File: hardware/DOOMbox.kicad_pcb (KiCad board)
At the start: 4 copper layers, 129 parts, among them J1 DE15_Socket_HighDensity, J2 AudioJack3, SW1 SW_SPST, SW2 SW_Push, U1 RPi Pico 2, U3 AP7381-50SA-7, U4 LM324N, U5 CD4010BE

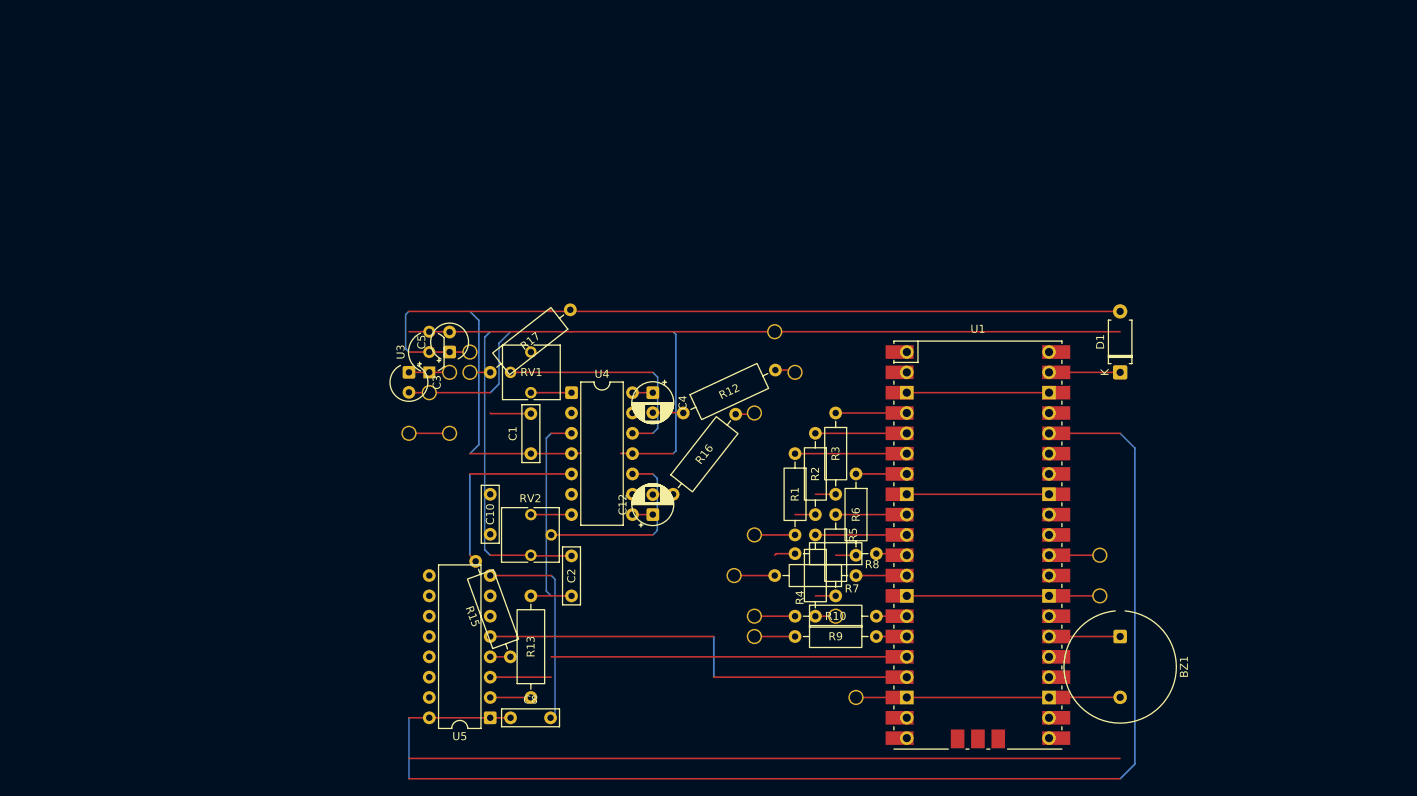
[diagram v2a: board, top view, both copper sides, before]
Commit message: Rework stripboard design (+ edit sb symbols)
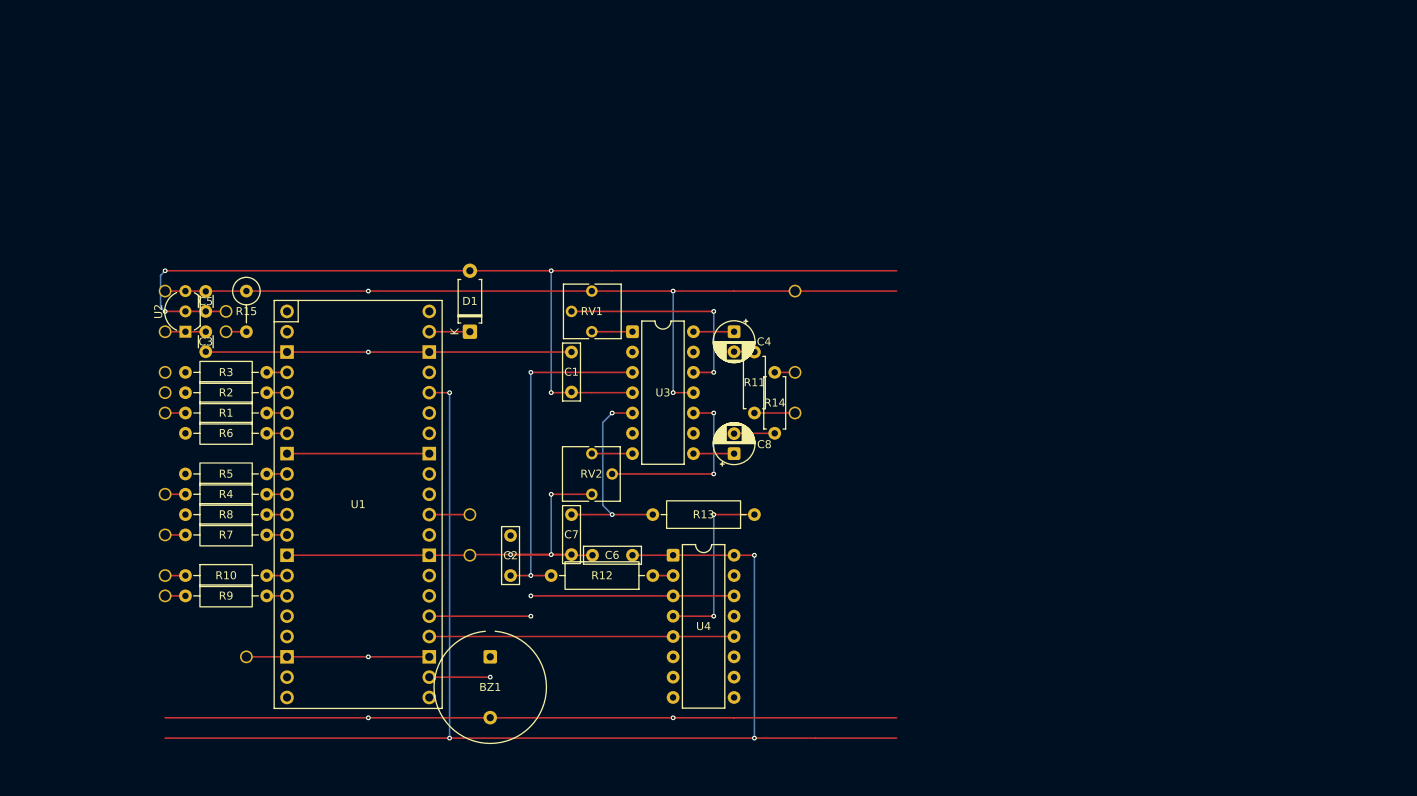
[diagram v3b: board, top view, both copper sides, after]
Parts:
- removed ? (x5): , 
- removed C10: 8n2, Capacitor_THT:C_Rect_L7.0mm_W2.0mm_P5.00mm
- removed C12: 4u7, Capacitor_THT:CP_Radial_D5.0mm_P2.50mm
- removed the D2 at (88.9, 66.0)
- removed the J1 at (124.5, 86.4)
- removed the J2 at (127.0, 61.0)
- removed the J2 at (124.5, 71.1)
- removed R16: 10K, Resistor_THT:R_Axial_DIN0309_L9.0mm_D3.2mm_P12.70mm_Horizontal
- removed R17: 15K, Resistor_THT:R_Axial_DIN0309_L9.0mm_D3.2mm_P12.70mm_Horizontal
- removed the REF** at (88.9, 63.5)
- removed the REF** at (126.1, 88.9)
- removed the REF** at (104.1, 83.8)
- removed the REF** at (121.9, 99.1)
- removed the REF** at (154.9, 76.2)
- removed the REF** at (154.9, 99.1)
- removed the REF** at (138.0, 99.0)
- removed the REF** at (154.9, 104.1)
- removed the REF** at (81.3, 73.7)
- removed the REF** at (114.3, 83.8)
- removed the REF** at (154.9, 86.4)
- removed the REF** at (131.1, 81.3)
- removed the REF** at (114.3, 68.6)
- removed the REF** at (133.4, 83.8)
- removed the REF** at (154.9, 109.2)
- removed the REF** at (154.9, 71.1)
- removed the REF** at (110.5, 71.1)
- removed the REF** at (116.8, 81.3)
- removed the REF** at (87.6, 91.4)
- removed the REF** at (119.4, 91.4)
- removed the REF** at (154.9, 96.5)
- removed the REF** at (93.0, 86.3)
- removed the REF** at (129.5, 94.0)
- removed the REF** at (87.6, 106.7)
- removed the REF** at (87.6, 101.6)
- removed the REF** at (114.3, 73.7)
- removed the REF** at (130.7, 86.4)
- removed the REF** at (121.9, 86.4)
- removed the REF** at (133.5, 88.9)
- removed the REF** at (94.0, 63.5)
- removed the REF** at (92.9, 66.1)
- removed the REF** at (110.8, 81.3)
- removed the REF** at (132.1, 91.4)
- removed the REF** at (114.3, 78.7)
- removed the REF** at (154.9, 63.5)
- removed the REF** at (87.6, 94.0)
- removed the REF** at (132.1, 66.0)
- removed the REF** at (121.9, 96.5)
- removed the REF** at (116.8, 71.1)
- removed the REF** at (149.9, 63.5)
- removed the REF** at (138.0, 96.5)
- removed the REF** at (88.9, 73.7)
- removed the REF** at (87.6, 96.5)
- removed the REF** at (137.2, 94.0)
- removed the REF** at (87.6, 99.1)
- removed the REF** at (154.9, 88.9)
- removed the REF** at (116.8, 76.2)
- removed the REF** at (101.6, 104.1)
- removed the REF** at (128.4, 83.9)
- removed the REF** at (154.9, 101.6)
- removed the REF** at (100.0, 71.0)
- removed the REF** at (136.2, 78.7)
- removed the REF** at (154.9, 91.4)
- removed the REF** at (101.6, 109.2)
- removed the REF** at (99.1, 63.5)
- removed the REF** at (86.4, 66.0)
- removed the REF** at (130.9, 96.5)
- removed the REF** at (104.1, 68.6)
- removed the REF** at (92.7, 96.5)
- removed the REF** at (130.6, 73.6)
- removed the REF** at (101.6, 106.7)
- removed the REF** at (154.9, 66.0)
- removed the REF** at (87.6, 104.1)
- removed the REF** at (157.5, 111.8)
- removed the REF** at (87.4, 66.1)
- removed the REF** at (104.1, 76.2)
- removed the REF** at (167.6, 94.0)
- removed the REF** at (149.9, 66.0)
- removed the REF** at (114.3, 66.0)
- removed the REF** at (154.9, 73.7)
- removed the REF** at (94.0, 68.6)
- removed the REF** at (100.2, 81.3)
- removed the REF** at (133.3, 71.1)
- removed the REF** at (92.5, 94.0)
- removed the REF** at (90.3, 89.0)
- removed the REF** at (83.8, 68.6)
- removed the REF** at (104.1, 73.7)
- removed the REF** at (84.9, 111.8)
- removed the REF** at (135.8, 91.5)
- removed the REF** at (154.9, 83.8)
- removed the REF** at (138.7, 88.7)
- removed the REF** at (154.9, 78.7)
- removed the REF** at (104.1, 81.3)
- removed the REF** at (128.3, 76.2)
- removed the SW1 at (86.4, 73.7)
- removed U5: CD4010BE, Package_DIP:DIP-16_W7.62mm
- added C6: 100n, Capacitor_THT:C_Rect_L7.0mm_W2.0mm_P5.00mm, F.Cu at (109.2, 88.9)
- added C7: 8n2, Capacitor_THT:C_Rect_L7.0mm_W2.0mm_P5.00mm, F.Cu at (101.6, 83.8)
- added D2: LED, Stripboard:Peripheral_Offboard, F.Cu at (58.4, 58.4)
- added D2: LED, Stripboard:Peripheral_Offboard, F.Cu at (58.4, 61.0)
- added J1: DE15_Socket_HighDensity, Stripboard:Peripheral_Offboard, F.Cu at (50.8, 86.4)
- added J1: DE15_Socket_HighDensity, Stripboard:Peripheral_Offboard, F.Cu at (50.8, 94.0)
- added J1: DE15_Socket_HighDensity, Stripboard:Peripheral_Offboard, F.Cu at (50.8, 71.1)
- added J1: DE15_Socket_HighDensity, Stripboard:Peripheral_Offboard, F.Cu at (50.8, 91.4)
- added J1: DE15_Socket_HighDensity, Stripboard:Peripheral_Offboard, F.Cu at (50.8, 81.3)
- added J1: DE15_Socket_HighDensity, Stripboard:Peripheral_Offboard, F.Cu at (61.0, 101.6)
- added J2: AudioJack3, Stripboard:Peripheral_Offboard, F.Cu at (129.5, 71.1)
- added J2: AudioJack3, Stripboard:Peripheral_Offboard, F.Cu at (129.5, 55.9)
- added R11: 10K, Resistor_THT:R_Axial_DIN0207_L6.3mm_D2.5mm_P7.62mm_Horizontal, F.Cu at (124.5, 63.5)
- added R14: 10K, Resistor_THT:R_Axial_DIN0207_L6.3mm_D2.5mm_P7.62mm_Horizontal, F.Cu at (127.0, 73.7)
- added REF**: Stripboard_Cut, Stripboard:Stripboard_Cut, F.Cu at (96.5, 68.6)
- added REF**: Stripboard_Cut, Stripboard:Stripboard_Cut, F.Cu at (116.8, 83.8)
- added REF**: Stripboard_Cut, Stripboard:Stripboard_Cut, F.Cu at (111.8, 68.6)
- added REF**: Stripboard_Cut, Stripboard:Stripboard_Cut, F.Cu at (73.7, 104.1)
- added REF**: Stripboard_Cut, Stripboard:Stripboard_Cut, F.Cu at (116.8, 106.7)
- added REF**: Peripheral_Offboard, Stripboard:Peripheral_Offboard, F.Cu at (50.8, 55.9)
- added REF**: Stripboard_Cut, Stripboard:Stripboard_Cut, F.Cu at (121.9, 71.1)
- added REF**: Stripboard_Cut, Stripboard:Stripboard_Cut, F.Cu at (106.7, 63.5)
- added REF**: Stripboard_Cut, Stripboard:Stripboard_Cut, F.Cu at (58.4, 86.4)
- added REF**: Peripheral_Offboard, Stripboard:Peripheral_Offboard, F.Cu at (50.8, 68.6)
- added REF**: Stripboard_Cut, Stripboard:Stripboard_Cut, F.Cu at (111.8, 101.6)
- added REF**: Stripboard_Cut, Stripboard:Stripboard_Cut, F.Cu at (86.4, 58.4)
- added REF**: Stripboard_Cut, Stripboard:Stripboard_Cut, F.Cu at (61.0, 58.4)
- added REF**: Stripboard_Cut, Stripboard:Stripboard_Cut, F.Cu at (101.6, 61.0)
- added REF**: Stripboard_Cut, Stripboard:Stripboard_Cut, F.Cu at (91.4, 91.4)
- added REF**: Stripboard_Cut, Stripboard:Stripboard_Cut, F.Cu at (86.4, 66.0)
- added REF**: Stripboard_Cut, Stripboard:Stripboard_Cut, F.Cu at (78.7, 106.7)
- added REF**: Stripboard_Cut, Stripboard:Stripboard_Cut, F.Cu at (78.7, 104.1)
- added REF**: Stripboard_Cut, Stripboard:Stripboard_Cut, F.Cu at (76.2, 94.0)
- added REF**: Stripboard_Cut, Stripboard:Stripboard_Cut, F.Cu at (78.7, 58.4)
- added REF**: Stripboard_Cut, Stripboard:Stripboard_Cut, F.Cu at (119.4, 73.7)
- added REF**: Stripboard_Cut, Stripboard:Stripboard_Cut, F.Cu at (106.7, 88.9)
- added REF**: Stripboard_Cut, Stripboard:Stripboard_Cut, F.Cu at (111.8, 96.5)
- added REF**: Stripboard_Cut, Stripboard:Stripboard_Cut, F.Cu at (58.4, 73.7)
- added REF**: Stripboard_Cut, Stripboard:Stripboard_Cut, F.Cu at (116.8, 101.6)
- added REF**: Stripboard_Cut, Stripboard:Stripboard_Cut, F.Cu at (76.2, 68.6)
- added REF**: Stripboard_Cut, Stripboard:Stripboard_Cut, F.Cu at (111.8, 73.7)
- added REF**: Stripboard_Cut, Stripboard:Stripboard_Cut, F.Cu at (111.8, 104.1)
- added REF**: Stripboard_Cut, Stripboard:Stripboard_Cut, F.Cu at (76.2, 66.0)
- added REF**: Stripboard_Cut, Stripboard:Stripboard_Cut, F.Cu at (116.8, 96.5)
- added REF**: Stripboard_Cut, Stripboard:Stripboard_Cut, F.Cu at (116.8, 91.4)
- added REF**: Stripboard_Cut, Stripboard:Stripboard_Cut, F.Cu at (111.8, 106.7)
- added REF**: Stripboard_Cut, Stripboard:Stripboard_Cut, F.Cu at (116.8, 99.1)
- added REF**: Stripboard_Cut, Stripboard:Stripboard_Cut, F.Cu at (121.9, 66.0)
- added REF**: Peripheral_Offboard, Stripboard:Peripheral_Offboard, F.Cu at (88.9, 88.9)
- added REF**: Stripboard_Cut, Stripboard:Stripboard_Cut, F.Cu at (78.7, 61.0)
- added REF**: Stripboard_Cut, Stripboard:Stripboard_Cut, F.Cu at (58.4, 68.6)
- added REF**: Stripboard_Cut, Stripboard:Stripboard_Cut, F.Cu at (91.4, 86.4)
- added REF**: Stripboard_Cut, Stripboard:Stripboard_Cut, F.Cu at (99.1, 83.8)
- added REF**: Stripboard_Cut, Stripboard:Stripboard_Cut, F.Cu at (58.4, 78.7)
- added REF**: Stripboard_Cut, Stripboard:Stripboard_Cut, F.Cu at (94.0, 94.0)
- added REF**: Stripboard_Cut, Stripboard:Stripboard_Cut, F.Cu at (101.6, 76.2)
- added REF**: Stripboard_Cut, Stripboard:Stripboard_Cut, F.Cu at (76.2, 78.7)
- added REF**: Stripboard_Cut, Stripboard:Stripboard_Cut, F.Cu at (116.8, 104.1)
- added REF**: Stripboard_Cut, Stripboard:Stripboard_Cut, F.Cu at (73.7, 58.4)
- added REF**: Stripboard_Cut, Stripboard:Stripboard_Cut, F.Cu at (111.8, 61.2)
- added REF**: Stripboard_Cut, Stripboard:Stripboard_Cut, F.Cu at (119.4, 63.5)
- added REF**: Stripboard_Cut, Stripboard:Stripboard_Cut, F.Cu at (55.9, 76.2)
- added REF**: Stripboard_Cut, Stripboard:Stripboard_Cut, F.Cu at (58.4, 91.4)
- added REF**: Stripboard_Cut, Stripboard:Stripboard_Cut, F.Cu at (106.7, 73.7)
- added REF**: Stripboard_Cut, Stripboard:Stripboard_Cut, F.Cu at (76.2, 91.4)
- added REF**: Stripboard_Cut, Stripboard:Stripboard_Cut, F.Cu at (73.7, 106.7)
- added REF**: Stripboard_Cut, Stripboard:Stripboard_Cut, F.Cu at (76.2, 96.5)
- added REF**: Stripboard_Cut, Stripboard:Stripboard_Cut, F.Cu at (111.8, 66.0)
- added REF**: Stripboard_Cut, Stripboard:Stripboard_Cut, F.Cu at (58.4, 94.0)
- added REF**: Stripboard_Cut, Stripboard:Stripboard_Cut, F.Cu at (52.1, 66.0)
- added REF**: Stripboard_Cut, Stripboard:Stripboard_Cut, F.Cu at (58.4, 66.0)
- added REF**: Stripboard_Cut, Stripboard:Stripboard_Cut, F.Cu at (111.8, 63.5)
- added REF**: Stripboard_Cut, Stripboard:Stripboard_Cut, F.Cu at (76.2, 86.4)
- added REF**: Stripboard_Cut, Stripboard:Stripboard_Cut, F.Cu at (76.2, 73.7)
- added REF**: Stripboard_Cut, Stripboard:Stripboard_Cut, F.Cu at (76.2, 99.1)
- added REF**: Stripboard_Cut, Stripboard:Stripboard_Cut, F.Cu at (111.8, 76.2)
- added REF**: Stripboard_Cut, Stripboard:Stripboard_Cut, F.Cu at (111.8, 71.1)
- added REF**: Stripboard_Cut, Stripboard:Stripboard_Cut, F.Cu at (116.8, 94.0)
- added REF**: Stripboard_Cut, Stripboard:Stripboard_Cut, F.Cu at (52.1, 68.5)
- added REF**: Stripboard_Cut, Stripboard:Stripboard_Cut, F.Cu at (62.1, 61.0)
- added REF**: Stripboard_Cut, Stripboard:Stripboard_Cut, F.Cu at (58.4, 81.3)
- added REF**: Stripboard_Cut, Stripboard:Stripboard_Cut, F.Cu at (58.4, 83.8)
- added REF**: Stripboard_Cut, Stripboard:Stripboard_Cut, F.Cu at (96.5, 81.3)
- added REF**: Stripboard_Cut, Stripboard:Stripboard_Cut, F.Cu at (57.1, 60.9)
- added REF**: Stripboard_Cut, Stripboard:Stripboard_Cut, F.Cu at (76.2, 81.3)
- added REF**: Stripboard_Cut, Stripboard:Stripboard_Cut, F.Cu at (88.9, 101.6)
- added REF**: Stripboard_Cut, Stripboard:Stripboard_Cut, F.Cu at (58.4, 71.1)
- added REF**: Stripboard_Cut, Stripboard:Stripboard_Cut, F.Cu at (76.2, 83.8)
- added REF**: Stripboard_Cut, Stripboard:Stripboard_Cut, F.Cu at (76.2, 71.1)
- added REF**: Stripboard_Cut, Stripboard:Stripboard_Cut, F.Cu at (73.7, 61.0)
- added SW1: SW_SPST, Stripboard:Peripheral_Offboard, F.Cu at (50.8, 66.0)
- added SW1: SW_SPST, Stripboard:Peripheral_Offboard, F.Cu at (50.8, 61.0)
- added U2: AP7381-50SA-7, Package_TO_SOT_THT:TO-92_Inline_Wide, F.Cu at (53.3, 61.0)
- C3, C5: footprint Capacitor_THT:CP_Radial_Tantal_D4.5mm_P2.50mm -> Capacitor_THT:C_Disc_D3.0mm_W1.6mm_P2.50mm
- C8: value 100n -> 4u7; footprint Capacitor_THT:C_Rect_L7.0mm_W2.0mm_P5.00mm -> Capacitor_THT:CP_Radial_D5.0mm_P2.50mm
- R12: value 10K -> 826R
- R15: value 826R -> 15K; footprint Resistor_THT:R_Axial_DIN0309_L9.0mm_D3.2mm_P12.70mm_Horizontal -> Resistor_THT:R_Axial_DIN0309_L9.0mm_D3.2mm_P5.08mm_Vertical
- U3: value AP7381-50SA-7 -> LM324N; footprint Package_TO_SOT_THT:TO-92_Inline_Wide -> Package_DIP:DIP-14_W7.62mm
- U4: value LM324N -> CD4010BE; footprint Package_DIP:DIP-14_W7.62mm -> Package_DIP:DIP-16_W7.62mm
- moved D1 81.4 mm to (88.9, 61.0)
- moved SW2 78.9 mm to (88.9, 83.8)
- moved BZ1 78.8 mm to (91.4, 101.6)
- moved U1 77.6 mm to (74.9, 82.5)
- moved R10 76.4 mm to (53.3, 91.4)
- moved R9 76.4 mm to (53.3, 94.0)
- moved R8 76.4 mm to (63.5, 83.8)
- moved R6 73.8 mm to (63.5, 73.7), turned to 180 degrees
- moved R7 73.8 mm to (63.5, 86.4)
- moved R3 71.3 mm to (63.5, 66.0), turned to 180 degrees
- moved R5 71.3 mm to (63.5, 78.7), turned to 180 degrees
- moved R2 68.8 mm to (63.5, 68.6), turned to 180 degrees
- moved R4 68.8 mm to (63.5, 81.3), turned to 180 degrees
- moved R1 66.2 mm to (63.5, 71.1), turned to 180 degrees
- moved R15 56.4 mm to (61.0, 55.9), turned to -90 degrees
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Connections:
- C2 pad 1: Net-(U4A-+) -> Net-(U3A-+)
- C4 pad 1: Net-(U4D--) -> Net-(U3D--)
- C4 pad 2: (no net) -> Net-(C4-Pad2)
- C8 pad 1: +3V3 -> Net-(U3C--)
- C8 pad 2: GND -> Net-(C8-Pad2)
- R12 pad 1: (no net) -> Net-(U4-G)
- R12 pad 2: (no net) -> Net-(U3A-+)
- R13 pad 1: Net-(U5-G) -> Net-(U4-H)
- R13 pad 2: Net-(U4A-+) -> Net-(U3B-+)
- R15 pad 1: Net-(U5-H) -> GND
- R15 pad 2: (no net) -> Net-(D2-K)
- RV1 pad 1: (no net) -> GND
- RV1 pad 2: (no net) -> Net-(U3D-+)
- RV1 pad 3: Net-(U4A--) -> Net-(U3A--)
- RV2 pad 2: (no net) -> Net-(U3C-+)
- RV2 pad 3: Net-(U4B--) -> Net-(U3B--)
- U1 pad 16: PWM_AUL -> unconnected-(U1-GPIO12-Pad16)
- U1 pad 17: PWM_AUR -> unconnected-(U1-GPIO13-Pad17)
- U1 pad 22: unconnected-(U1-GPIO17-Pad22) -> Net-(BZ1-+)
- U1 pad 24: unconnected-(U1-GPIO18-Pad24) -> PWM_AUR
- U1 pad 25: unconnected-(U1-GPIO19-Pad25) -> PWM_AUL
- U1 pad 26: Net-(BZ1-+) -> unconnected-(U1-GPIO20-Pad26)
- U3 pad 1: Net-(SW1-B) -> Net-(U3A--)
- U3 pad 2: +5V -> Net-(U3A--)
- U3 pad 3: GND -> Net-(U3A-+)
- U4 pad 1: Net-(U4A--) -> +3V3
- U4 pad 10: Net-(U4C-+) -> unconnected-(U4-J-Pad10)
- U4 pad 11: GND -> unconnected-(U4-E-Pad11)
- U4 pad 12: Net-(U4D-+) -> unconnected-(U4-K-Pad12)
- U4 pad 13: Net-(U4D--) -> unconnected-(U4-NC-Pad13)
- U4 pad 14: Net-(U4D--) -> unconnected-(U4-F-Pad14)
- U4 pad 2: Net-(U4A--) -> Net-(U4-G)
- U4 pad 3: Net-(U4A-+) -> PWM_AUL
- U4 pad 4: +5V -> Net-(U4-H)
- U4 pad 5: Net-(U4B-+) -> PWM_AUR
- U4 pad 6: Net-(U4B--) -> unconnected-(U4-I-Pad6)
- U4 pad 7: Net-(U4B--) -> unconnected-(U4-C-Pad7)
- U4 pad 8: Net-(U4C--) -> GND
- U4 pad 9: Net-(U4C--) -> unconnected-(U4-D-Pad9)
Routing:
- net GND: track 484.8 -> 363.3 mm, vias 0 -> 10
- net (no net): track 118.3 -> 0.00 mm
- net +5V: track 21.5 -> 130.0 mm, vias 0 -> 4
- net +3V3: track 110.5 -> 175.3 mm, vias 0 -> 4
- net Net-(U3A-+): track 0.00 -> 43.2 mm, vias 0 -> 2
- net Net-(U4D--): track 32.6 -> 0.00 mm
- net Net-(U3D-+): track 0.00 -> 27.9 mm, vias 0 -> 2
- net Net-(U3B-+): track 0.00 -> 26.4 mm, vias 0 -> 2
- net Net-(U4-H): track 0.00 -> 22.9 mm, vias 0 -> 2
- net Net-(U3C-+): track 0.00 -> 22.9 mm, vias 0 -> 2
- net Net-(D2-K): track 21.2 -> 2.54 mm
- net Net-(U4C--): track 15.7 -> 0.00 mm
- net Net-(U4B-+): track 15.2 -> 0.00 mm
- net PWM_AUR: track 52.1 -> 38.1 mm
- net VGA_R2: track 14.0 -> 2.54 mm
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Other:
- board text added: "+"
- board text added: "-"
- board text added: "J1"
- board text added: "J2.R"
- board text added: "J2.S"
- board text added: "J2.T"
- board text removed: "J2"
- board text removed: "R7, R8 on top + horiz"

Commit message: Shorten R12 and R13 + add missing cut
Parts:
- added REF**: Stripboard_Cut, Stripboard:Stripboard_Cut, F.Cu at (106.7, 91.4)
- R12: footprint Resistor_THT:R_Axial_DIN0309_L9.0mm_D3.2mm_P12.70mm_Horizontal -> Resistor_THT:R_Axial_DIN0207_L6.3mm_D2.5mm_P10.16mm_Horizontal
- R13: footprint Resistor_THT:R_Axial_DIN0309_L9.0mm_D3.2mm_P12.70mm_Horizontal -> Resistor_THT:R_Axial_DIN0207_L6.3mm_D2.5mm_P7.62mm_Horizontal
- moved R13 7.62 mm to (116.8, 83.8)
- moved REF** 2.54 mm to (114.3, 83.8)
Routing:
- net Net-(U4-H): track 22.9 -> 20.3 mm
- net Net-(U3B-+): track 26.4 -> 23.8 mm
- net Net-(U3A-+): track 43.2 -> 45.7 mm
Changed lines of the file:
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@@
 	(footprint "Stripboard:Stripboard_Cut"
 		(layer "F.Cu")
-		(at 116.84 83.82)
+		(at 114.3 83.82)
 		(descr "A cut mark in a copper strip")
 		(property "Reference" "REF**"
@@
 	(footprint "Stripboard:Stripboard_Cut"
 		(layer "F.Cu")
+		(at 106.68 91.44)
+		(descr "A cut mark in a copper strip")
+		(property "Reference" "REF**"
+			(at 0 -6.58 0)
+			(unlocked yes)
+			(layer "F.SilkS")
+			(hide yes)
+			(effects
+				(font
+					(size 1 1)
+					(thickness 0.1)
+				)
+			)
+		)
+		(property "Value" "Stripboard_Cut"
+			(at 0 -5.08 0)
+			(unlocked yes)
+			(layer "F.Fab")
+			(hide yes)
+			(effects
+				(font
+					(size 1 1)
+					(thickness 0.15)
+				)
+			)
+		)
+		(property "Datasheet" ""
+			(at 0 0 0)
+			(unlocked yes)
+			(layer "F.Fab")
+			(hide yes)
+			(effects
+				(font
+					(size 1 1)
+					(thickness 0.15)
+				)
+			)
+		)
+		(property "Description" "A cut mark in a copper strip"
+			(at 0 0 0)
+			(unlocked yes)
+			(layer "F.Fab")
+			(hide yes)
+			(effects
+				(font
+					(size 1 1)
+					(thickness 0.15)
+				)
+			)
+		)
+		(attr smd)
+		(fp_line
+			(start -0.636396 -0.636396)
+			(end 0.636396 0.636396)
+			(stroke
+				(width 0.2)
+				(type solid)
+			)
+			(layer "B.Paste")
+		)
+		(fp_line
+			(start 0.636396 -0.636396)
+			(end -0.636396 0.636396)
+			(stroke
+				(width 0.2)
+				(type solid)
+			)
+			(layer "B.Paste")
+		)
+		(embedded_fonts no)
+	)
+	(footprint "Stripboard:Stripboard_Cut"
+		(layer "F.Cu")
 		(at 101.6 60.96)
 		(descr "A cut mark in a copper strip")
@@
 		(embedded_fonts no)
 	)
-	(footprint "Resistor_THT:R_Axial_DIN0309_L9.0mm_D3.2mm_P12.70mm_Horizontal"
+	(footprint "Resistor_THT:R_Axial_DIN0207_L6.3mm_D2.5mm_P10.16mm_Horizontal"
 		(layer "F.Cu")
 		(at 111.76 91.44 180)
-		(descr "Resistor, Axial_DIN0309 series, Axial, Horizontal, pin pitch=12.7mm, 0.5W = 1/2W, length*diameter=9*3.2mm^2, http://cdn-reichelt.de/documents/datenblatt/B400/1_4W%23YAG.pdf")
-		(tags "Resistor Axial_DIN0309 series Axial Horizontal pin pitch 12.7mm 0.5W = 1/2W length 9mm diameter 3.2mm")
+		(descr "Resistor, Axial_DIN0207 series, Axial, Horizontal, pin pitch=10.16mm, 0.25W = 1/4W, length*diameter=6.3*2.5mm^2, http://cdn-reichelt.de/documents/datenblatt/B400/1_4W%23YAG.pdf")
+		(tags "Resistor Axial_DIN0207 series Axial Horizontal pin pitch 10.16mm 0.25W = 1/4W length 6.3mm diameter 2.5mm")
 		(property "Reference" "R12"
-			(at 6.35 0 0)
+			(at 5.08 0 180)
 			(layer "F.SilkS")
 			(effects
@@
 		)
 		(property "Value" "826R"
-			(at 6.35 2.72 0)
+			(at 5.08 2.37 180)
 			(layer "F.Fab")
 			(effects
@@
 			)
 		)
-		(property "Datasheet" "~"
-			(at 0 0 0)
+		(property "Datasheet" ""
+			(at 0 0 180)
 			(layer "F.Fab")
 			(hide yes)
@@
 			)
 		)
-		(property "Description" "Resistor"
-			(at 0 0 0)
+		(property "Description" ""
+			(at 0 0 180)
 			(layer "F.Fab")
 			(hide yes)
@@
 		(attr through_hole)
 		(fp_line
-			(start 11.66 0)
-			(end 10.97 0)
+			(start 9.12 0)
+			(end 8.35 0)
 			(stroke
 				(width 0.12)
@@
 		(fp_line
 			(start 1.04 0)
-			(end 1.73 0)
+			(end 1.81 0)
 			(stroke
 				(width 0.12)
@@
 		)
 		(fp_rect
-			(start 1.73 -1.72)
-			(end 10.97 1.72)
+			(start 1.81 -1.37)
+			(end 8.35 1.37)
 			(stroke
 				(width 0.12)
@@
 		)
 		(fp_rect
-			(start -1.05 -1.85)
-			(end 13.75 1.85)
+			(start -1.05 -1.5)
+			(end 11.21 1.5)
 			(stroke
 				(width 0.05)
@@
 		)
 		(fp_line
-			(start 12.7 0)
-			(end 10.85 0)
+			(start 10.16 0)
+			(end 8.23 0)
 			(stroke
 				(width 0.1)
@@
 		(fp_line
 			(start 0 0)
-			(end 1.85 0)
+			(end 1.93 0)
 			(stroke
 				(width 0.1)
@@
 		)
 		(fp_rect
-			(start 1.85 -1.6)
-			(end 10.85 1.6)
+			(start 1.93 -1.25)
+			(end 8.23 1.25)
 			(stroke
 				(width 0.1)
@@
 		)
 		(fp_text user "${REFERENCE}"
-			(at 6.35 0 0)
+			(at 5.08 0 180)
 			(layer "F.Fab")
 			(effects
@@
 		)
 		(pad "2" thru_hole circle
-			(at 12.7 0 180)
+			(at 10.16 0 180)
 			(size 1.6 1.6)
 			(drill 0.8)
@@
 		)
 		(embedded_fonts no)
-		(model "${KICAD9_3DMODEL_DIR}/Resistor_THT.3dshapes/R_Axial_DIN0309_L9.0mm_D3.2mm_P12.70mm_Horizontal.step"
+		(model "${KICAD9_3DMODEL_DIR}/Resistor_THT.3dshapes/R_Axial_DIN0207_L6.3mm_D2.5mm_P10.16mm_Horizontal.step"
 			(offset
 				(xyz 0 0 0)
@@
 		(embedded_fonts no)
 	)
-	(footprint "Resistor_THT:R_Axial_DIN0309_L9.0mm_D3.2mm_P12.70mm_Horizontal"
+	(footprint "Resistor_THT:R_Axial_DIN0207_L6.3mm_D2.5mm_P7.62mm_Horizontal"
 		(layer "F.Cu")
-		(at 124.46 83.82 180)
-		(descr "Resistor, Axial_DIN0309 series, Axial, Horizontal, pin pitch=12.7mm, 0.5W = 1/2W, length*diameter=9*3.2mm^2, http://cdn-reichelt.de/documents/datenblatt/B400/1_4W%23YAG.pdf")
-		(tags "Resistor Axial_DIN0309 series Axial Horizontal pin pitch 12.7mm 0.5W = 1/2W length 9mm diameter 3.2mm")
+		(at 116.84 83.82 180)
+		(descr "Resistor, Axial_DIN0207 series, Axial, Horizontal, pin pitch=7.62mm, 0.25W = 1/4W, length*diameter=6.3*2.5mm^2, http://cdn-reichelt.de/documents/datenblatt/B400/1_4W%23YAG.pdf")
+		(tags "Resistor Axial_DIN0207 series Axial Horizontal pin pitch 7.62mm 0.25W = 1/4W length 6.3mm diameter 2.5mm")
 		(property "Reference" "R13"
-			(at 6.35 0 180)
+			(at 3.81 0 180)
 			(layer "F.SilkS")
 			(effects
@@
 		)
 		(property "Value" "826R"
-			(at 6.35 2.72 0)
+			(at 3.81 2.37 180)
 			(layer "F.Fab")
 			(effects
@@
 			)
 		)
-		(property "Datasheet" "~"
-			(at 0 0 0)
+		(property "Datasheet" ""
+			(at 0 0 180)
 			(layer "F.Fab")
 			(hide yes)
@@
 			)
 		)
-		(property "Description" "Resistor"
-			(at 0 0 0)
+		(property "Description" ""
+			(at 0 0 180)
 			(layer "F.Fab")
 			(hide yes)
@@
 		(attr through_hole)
 		(fp_line
-			(start 11.66 0)
-			(end 10.97 0)
+			(start 7.08 1.37)
+			(end 7.08 1.04)
 			(stroke
 				(width 0.12)
@@
 		)
 		(fp_line
-			(start 1.04 0)
-			(end 1.73 0)
+			(start 7.08 -1.37)
+			(end 7.08 -1.04)
 			(stroke
 				(width 0.12)
@@
 			(layer "F.SilkS")
 		)
-		(fp_rect
-			(start 1.73 -1.72)
-			(end 10.97 1.72)
+		(fp_line
+			(start 0.54 1.37)
+			(end 7.08 1.37)
+			(stroke
+				(width 0.12)
+				(type solid)
+			)
+			(layer "F.SilkS")
+		)
+		(fp_line
+			(start 0.54 1.04)
+			(end 0.54 1.37)
+			(stroke
+				(width 0.12)
+				(type solid)
+			)
+			(layer "F.SilkS")
+		)
+		(fp_line
+			(start 0.54 -1.04)
+			(end 0.54 -1.37)
+			(stroke
+				(width 0.12)
+				(type solid)
+			)
+			(layer "F.SilkS")
+		)
+		(fp_line
+			(start 0.54 -1.37)
+			(end 7.08 -1.37)
 			(stroke
 				(width 0.12)
 				(type solid)
 			)
-			(fill no)
 			(layer "F.SilkS")
 		)
 		(fp_rect
-			(start -1.05 -1.85)
-			(end 13.75 1.85)
+			(start -1.05 -1.5)
+			(end 8.67 1.5)
 			(stroke
 				(width 0.05)
@@
 		)
 		(fp_line
-			(start 12.7 0)
-			(end 10.85 0)
+			(start 7.62 0)
+			(end 6.96 0)
 			(stroke
 				(width 0.1)
@@
 		(fp_line
 			(start 0 0)
-			(end 1.85 0)
+			(end 0.66 0)
 			(stroke
 				(width 0.1)
@@
 		)
 		(fp_rect
-			(start 1.85 -1.6)
-			(end 10.85 1.6)
+			(start 0.66 -1.25)
+			(end 6.96 1.25)
 			(stroke
 				(width 0.1)
@@
 		)
 		(fp_text user "${REFERENCE}"
-			(at 6.35 0 0)
+			(at 3.81 0 180)
 			(layer "F.Fab")
 			(effects
@@
 		)
 		(pad "2" thru_hole circle
-			(at 12.7 0 180)
+			(at 7.62 0 180)
 			(size 1.6 1.6)
 			(drill 0.8)
@@
 		)
 		(embedded_fonts no)
-		(model "${KICAD9_3DMODEL_DIR}/Resistor_THT.3dshapes/R_Axial_DIN0309_L9.0mm_D3.2mm_P12.70mm_Horizontal.step"
+		(model "${KICAD9_3DMODEL_DIR}/Resistor_THT.3dshapes/R_Axial_DIN0207_L6.3mm_D2.5mm_P7.62mm_Horizontal.step"
 			(offset
 				(xyz 0 0 0)
@@
 	)
 	(segment
-		(start 99.06 91.44)
+		(start 101.6 91.44)
 		(end 96.52 91.44)
 		(width 0.2)
@@
 	)
 	(segment
-		(start 111.76 83.82)
-		(end 106.68 83.82)
+		(start 106.68 83.82)
+		(end 101.6 83.82)
 		(width 0.2)
 		(layer "F.Cu")
@@
 	)
 	(segment
-		(start 106.68 83.82)
-		(end 101.6 83.82)
+		(start 109.22 71.12)
+		(end 106.68 71.12)
 		(width 0.2)
 		(layer "F.Cu")
@@
 	)
 	(segment
-		(start 109.22 71.12)
-		(end 106.68 71.12)
+		(start 109.22 83.82)
+		(end 106.68 83.82)
 		(width 0.2)
 		(layer "F.Cu")
@@
 	)
 	(segment
-		(start 124.46 83.82)
-		(end 119.38 83.82)
+		(start 119.38 83.82)
+		(end 116.84 83.82)
 		(width 0.2)
 		(layer "F.Cu")

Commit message: Organise stripboard layers + offboard SW1
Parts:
- removed the REF** at (50.8, 68.6)
- added REF**: Stripboard_Cut, Stripboard:Stripboard_Cut, F.Cu at (99.1, 96.5)
- added REF**: Stripboard_Cut, Stripboard:Stripboard_Cut, F.Cu at (94.0, 104.1)
- added REF**: Stripboard_Cut, Stripboard:Stripboard_Cut, F.Cu at (94.0, 101.6)
- added REF**: Stripboard_Cut, Stripboard:Stripboard_Cut, F.Cu at (99.1, 58.4)
- added SW1: SW_SPST, Stripboard:Peripheral_Offboard, F.Cu at (50.8, 61.0)
- moved SW1 14.0 mm to (40.8, 56.3)
- moved SW1 7.61 mm to (43.2, 60.5)
- moved REF** 5.08 mm to (88.9, 94.0)
- moved REF** 2.54 mm to (88.9, 91.4)
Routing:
- net VDC: track 2.54 -> 0.00 mm
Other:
- board text added: "CUT"
- board text added: "Cut if GPIO16 not used"
- board text added: "Cuts here if pins not used for input"
- board text added: "VDC"
- board text removed: "+"
- board text removed: "-"
